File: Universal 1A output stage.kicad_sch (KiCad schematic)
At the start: 58 parts, among them U306 LM317T, U307 LT3045xMSE, U308 LT3045xMSE, U309 78L05, U310 MP1584EN

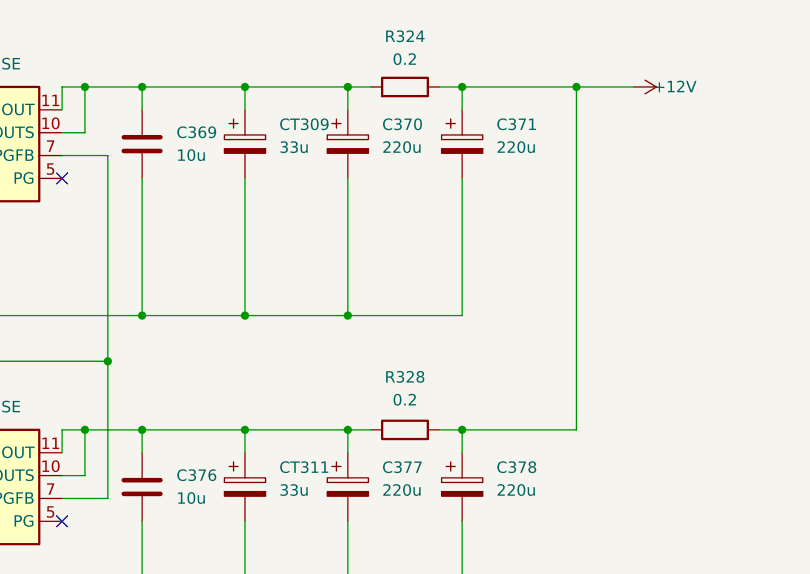
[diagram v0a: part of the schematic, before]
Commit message: correct resistor
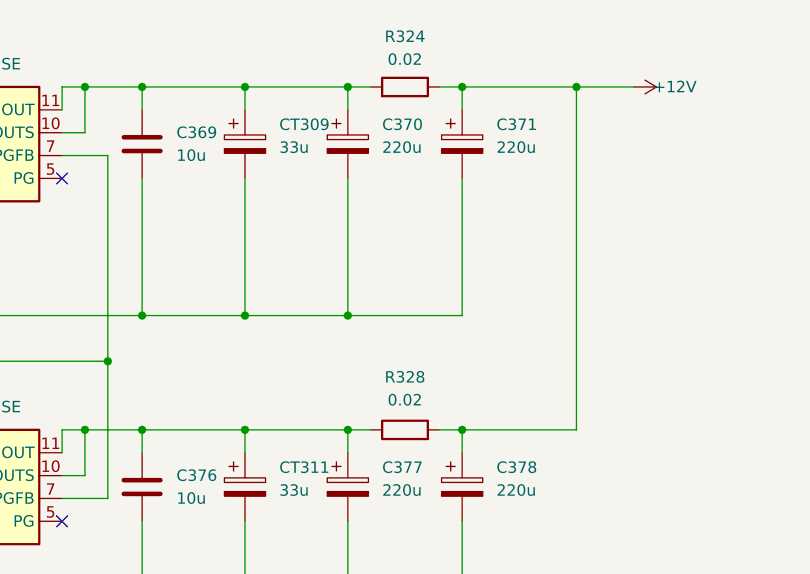
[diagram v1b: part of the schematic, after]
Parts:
- R324, R328: value 0.2 -> 0.02
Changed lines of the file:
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@@
 			)
 		)
-		(property "Value" "0.2"
+		(property "Value" "0.02"
 			(at 363.22 23.622 90)
 			(show_name no)
@@
 			)
 		)
-		(property "Value" "0.2"
+		(property "Value" "0.02"
 			(at 363.22 61.468 90)
 			(show_name no)

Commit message: Add connection testpoints and noise reduction capacitors
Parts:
- added C238, C239, C240: 2n2, symbol Device:C
- added SP10: ENABLE, symbol Connector:TestPoint
- added SP11: GND_in, symbol Connector:TestPoint
- added SP12: +12V_out, symbol Connector:TestPoint
- added SP13: GND_out, symbol Connector:TestPoint
- added SP9: +15V_in, symbol Connector:TestPoint
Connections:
- net +12V: now also C240.1, SP12.1
- net +15V: now also C238.1, SP9.1
- net ENABLE: now also C239.1, SP10.1
- net GND: now also C238.2, C239.2, C240.2, SP11.1, SP13.1

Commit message: capacitir add
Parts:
- added C390: 33p, symbol Device:C
- C389: value 150p -> 330p
- R336: value 147k -> 100k
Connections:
- net GND: now also C390.2
- net at C389.1, U310.3 (COMP): now also C390.1
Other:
- moved on the sheet: C389, R336, R337
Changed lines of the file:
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@@
 	)
 	(junction
+		(at 107.95 128.27)
+		(diameter 0)
+		(color 0 0 0 0)
+	)
+	(junction
 		(at 161.29 111.76)
 		(diameter 0)
@@
 	)
 	(junction
-		(at 149.86 111.76)
+		(at 115.57 128.27)
 		(diameter 0)
 		(color 0 0 0 0)
 	)
 	(junction
-		(at 265.43 64.77)
+		(at 149.86 111.76)
 		(diameter 0)
 		(color 0 0 0 0)
 	)
 	(junction
-		(at 60.96 81.28)
+		(at 265.43 64.77)
 		(diameter 0)
 		(color 0 0 0 0)
 	)
 	(junction
-		(at 109.22 128.27)
+		(at 60.96 81.28)
 		(diameter 0)
 		(color 0 0 0 0)
@@
 	)
 	(junction
-		(at 138.43 26.67)
+		(at 119.38 115.57)
 		(diameter 0)
 		(color 0 0 0 0)
 	)
 	(junction
-		(at 345.44 64.77)
+		(at 138.43 26.67)
 		(diameter 0)
 		(color 0 0 0 0)
 	)
 	(junction
-		(at 114.3 115.57)
+		(at 345.44 64.77)
 		(diameter 0)
 		(color 0 0 0 0)
@@
 	)
 	(junction
+		(at 107.95 106.68)
+		(diameter 0)
+		(color 0 0 0 0)
+	)
+	(junction
 		(at 265.43 52.07)
 		(diameter 0)
@@
 	(wire
 		(pts
-			(xy 109.22 125.73) (xy 109.22 128.27)
+			(xy 107.95 125.73) (xy 107.95 128.27)
 		)
 		(stroke
@@
 	(wire
 		(pts
+			(xy 115.57 109.22) (xy 115.57 106.68)
+		)
+		(stroke
+			(width 0)
+			(type default)
+		)
+	)
+	(wire
+		(pts
 			(xy 134.62 111.76) (xy 149.86 111.76)
 		)
@@
 	(wire
 		(pts
-			(xy 109.22 116.84) (xy 109.22 118.11)
+			(xy 107.95 116.84) (xy 107.95 118.11)
 		)
 		(stroke
@@
 	(wire
 		(pts
+			(xy 107.95 106.68) (xy 115.57 106.68)
+		)
+		(stroke
+			(width 0)
+			(type default)
+		)
+	)
+	(wire
+		(pts
 			(xy 242.57 36.83) (xy 242.57 52.07)
 		)
@@
 	(wire
 		(pts
+			(xy 107.95 128.27) (xy 115.57 128.27)
+		)
+		(stroke
+			(width 0)
+			(type default)
+		)
+	)
+	(wire
+		(pts
 			(xy 88.9 52.07) (xy 114.3 52.07)
 		)
@@
 	(wire
 		(pts
-			(xy 114.3 128.27) (xy 109.22 128.27)
+			(xy 119.38 128.27) (xy 115.57 128.27)
 		)
 		(stroke
@@
 	(wire
 		(pts
-			(xy 106.68 106.68) (xy 109.22 106.68)
+			(xy 106.68 106.68) (xy 107.95 106.68)
 		)
 		(stroke
@@
 	(wire
 		(pts
-			(xy 106.68 101.6) (xy 114.3 101.6)
+			(xy 106.68 101.6) (xy 119.38 101.6)
 		)
 		(stroke
@@
 	(wire
 		(pts
-			(xy 96.52 128.27) (xy 109.22 128.27)
+			(xy 96.52 128.27) (xy 107.95 128.27)
 		)
 		(stroke
@@
 	(wire
 		(pts
-			(xy 109.22 106.68) (xy 109.22 109.22)
+			(xy 107.95 106.68) (xy 107.95 109.22)
 		)
 		(stroke
@@
 	(wire
 		(pts
-			(xy 114.3 115.57) (xy 114.3 118.11)
+			(xy 119.38 115.57) (xy 119.38 118.11)
 		)
 		(stroke
@@
 	(wire
 		(pts
+			(xy 119.38 115.57) (xy 123.19 115.57)
+		)
+		(stroke
+			(width 0)
+			(type default)
+		)
+	)
+	(wire
+		(pts
 			(xy 314.96 41.91) (xy 314.96 52.07)
 		)
@@
 	(wire
 		(pts
-			(xy 114.3 115.57) (xy 123.19 115.57)
-		)
-		(stroke
-			(width 0)
-			(type default)
-		)
-	)
-	(wire
-		(pts
 			(xy 88.9 49.53) (xy 88.9 52.07)
 		)
@@
 	(wire
 		(pts
-			(xy 114.3 101.6) (xy 114.3 115.57)
+			(xy 119.38 101.6) (xy 119.38 115.57)
 		)
 		(stroke
@@
 	(wire
 		(pts
+			(xy 115.57 116.84) (xy 115.57 128.27)
+		)
+		(stroke
+			(width 0)
+			(type default)
+		)
+	)
+	(wire
+		(pts
 			(xy 76.2 39.37) (xy 76.2 41.91)
 		)
@@
 	(wire
 		(pts
-			(xy 114.3 125.73) (xy 114.3 128.27)
+			(xy 119.38 125.73) (xy 119.38 128.27)
 		)
 		(stroke
@@
 	(symbol
 		(lib_id "Device:R")
-		(at 109.22 121.92 0)
+		(at 107.95 121.92 0)
 		(mirror y)
 		(unit 1)
@@
 		(dnp no)
 		(property "Reference" "R336"
-			(at 106.68 120.6499 0)
+			(at 105.41 120.6499 0)
 			(show_name no)
 			(do_not_autoplace no)
@@
 			)
 		)
-		(property "Value" "147k"
-			(at 106.68 123.1899 0)
+		(property "Value" "100k"
+			(at 105.41 123.1899 0)
 			(show_name no)
 			(do_not_autoplace no)
@@
 		)
 		(property "Footprint" ""
-			(at 110.998 121.92 90)
+			(at 109.728 121.92 90)
 			(hide yes)
 			(show_name no)
@@
 		)
 		(property "Datasheet" ""
-			(at 109.22 121.92 0)
+			(at 107.95 121.92 0)
 			(hide yes)
 			(show_name no)
@@
 		)
 		(property "Description" "Resistor"
-			(at 109.22 121.92 0)
+			(at 107.95 121.92 0)
 			(hide yes)
 			(show_name no)
@@
 		)
 		(property "MPN" "RC0805FR-07147KL"
-			(at 109.22 121.92 0)
+			(at 107.95 121.92 0)
 			(hide yes)
 			(show_name no)
@@
 	(symbol
 		(lib_id "Device:R")
-		(at 114.3 121.92 0)
+		(at 119.38 121.92 0)
 		(unit 1)
 		(body_style 1)
@@
 		(in_pos_files yes)
 		(dnp no)
-		(fields_autoplaced yes)
 		(property "Reference" "R337"
-			(at 116.84 120.6499 0)
+			(at 121.412 123.19 0)
 			(show_name no)
 			(do_not_autoplace no)
@@
 		)
 		(property "Value" "19k6"
-			(at 116.84 123.1899 0)
+			(at 121.412 125.73 0)
 			(show_name no)
 			(do_not_autoplace no)
@@
 		)
 		(property "Footprint" ""
-			(at 112.522 121.92 90)
+			(at 117.602 121.92 90)
 			(hide yes)
 			(show_name no)
@@
 		)
 		(property "Datasheet" ""
-			(at 114.3 121.92 0)
+			(at 119.38 121.92 0)
 			(hide yes)
 			(show_name no)
@@
 		)
 		(property "Description" "Resistor"
-			(at 114.3 121.92 0)
+			(at 119.38 121.92 0)
 			(hide yes)
 			(show_name no)
@@
 		)
 		(property "MPN" "RC0805FR-0719K6L"
-			(at 114.3 121.92 0)
+			(at 119.38 121.92 0)
 			(hide yes)
 			(show_name no)
@@
 		(dnp no)
 		(property "Reference" "R335"
-			(at 124.714 119.38 90)
+			(at 127 118.872 90)
 			(show_name no)
 			(do_not_autoplace no)
@@
 		)
 		(property "Value" "300k"
-			(at 129.54 119.38 90)
+			(at 133.096 119.126 90)
 			(show_name no)
 			(do_not_autoplace no)
@@
 	(symbol
 		(lib_id "Device:C")
-		(at 109.22 113.03 0)
+		(at 107.95 113.03 0)
 		(mirror y)
 		(unit 1)
@@
 		(dnp no)
 		(property "Reference" "C389"
-			(at 105.41 111.7599 0)
+			(at 104.14 111.7599 0)
 			(show_name no)
 			(do_not_autoplace no)
@@
 			)
 		)
-		(property "Value" "150p"
-			(at 105.41 114.2999 0)
+		(property "Value" "330p"
+			(at 104.14 114.2999 0)
 			(show_name no)
 			(do_not_autoplace no)
@@
 		)
 		(property "Footprint" ""
-			(at 108.2548 116.84 0)
+			(at 106.9848 116.84 0)
 			(hide yes)
 			(show_name no)
@@
 		)
 		(property "Datasheet" ""
-			(at 109.22 113.03 0)
+			(at 107.95 113.03 0)
 			(hide yes)
 			(show_name no)
@@
 		)
 		(property "Description" "Unpolarized ceramic capacitor"
-			(at 109.22 113.03 0)
+			(at 107.95 113.03 0)
 			(hide yes)
 			(show_name no)
@@
 		)
 		(property "MPN" "CC0805JRNPO0BN151"
-			(at 109.22 113.03 0)
+			(at 107.95 113.03 0)
 			(hide yes)
 			(show_name no)
@@
 					(unit 1)
 				)
+			)
+		)
+	)
+	(symbol
+		(lib_id "Device:C")
+		(at 115.57 113.03 0)
+		(mirror y)
+		(unit 1)
+		(body_style 1)
+		(exclude_from_sim no)
+		(in_bom yes)
+		(on_board yes)
+		(in_pos_files yes)
+		(dnp no)
+		(property "Reference" "C390"
+			(at 115.062 115.824 0)
+			(show_name no)
+			(do_not_autoplace no)
+			(effects
+				(font
+					(size 1.27 1.27)
+				)
+				(justify left)
+			)
+		)
+		(property "Value" "33p"
+			(at 114.554 118.872 0)
+			(show_name no)
+			(do_not_autoplace no)
+			(effects
+				(font
+					(size 1.27 1.27)
+				)
+				(justify left)
+			)
+		)
+		(property "Footprint" ""
+			(at 114.6048 116.84 0)
+			(hide yes)
+			(show_name no)
+			(do_not_autoplace no)
+			(effects
+				(font
+					(size 1.27 1.27)
+				)
+			)
+		)
+		(property "Datasheet" ""
+			(at 115.57 113.03 0)
+			(hide yes)
+			(show_name no)
+			(do_not_autoplace no)
+			(effects
+				(font
+					(size 1.27 1.27)
+				)
+			)
+		)
+		(property "Description" "Unpolarized ceramic capacitor"
+			(at 115.57 113.03 0)
+			(hide yes)
+			(show_name no)
+			(do_not_autoplace no)
+			(effects
+				(font
+					(size 1.27 1.27)
+				)
+			)
+		)
+		(property "MPN" "CC0805JRNPO0BN151"
+			(at 115.57 113.03 0)
+			(hide yes)
+			(show_name no)
+			(do_not_autoplace no)
+			(effects
+				(font
+					(size 1.27 1.27)
+				)
+			)
+		)
+		(pin "1"
+		)
+		(pin "2"
+		)
+		(instances
+			(project "Low noise power supply"
+				(path "/fca69f12-2166-43a7-ac92-c50992f66d73/9f391ce8-5af9-46a1-8a20-7b36334a3f29"
+					(reference "C390")
+					(unit 1)
+				)
